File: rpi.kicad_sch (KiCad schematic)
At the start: 13 parts, among them J18 Raspberry_Pi_2_3, U1 AT24C256C, U16 MCP2518FD-xQBB, U19 SN65HVD230, Y2 40MHz

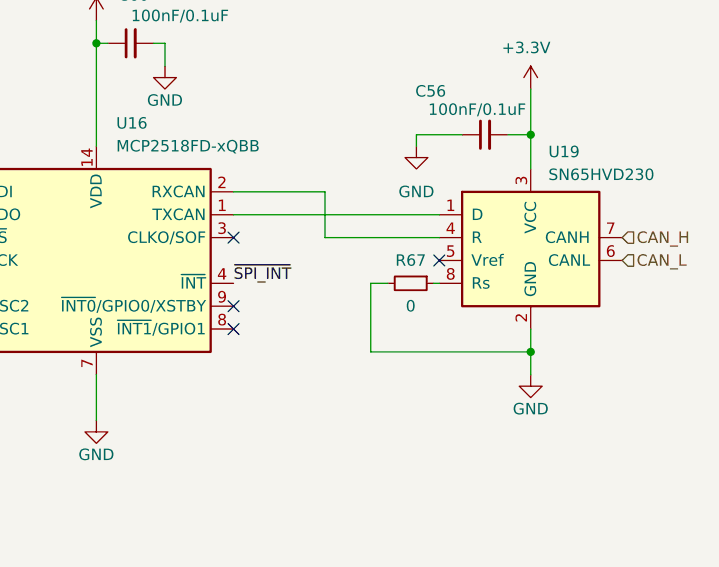
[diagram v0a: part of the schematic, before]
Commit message: Fix ERC errors
Closes #28
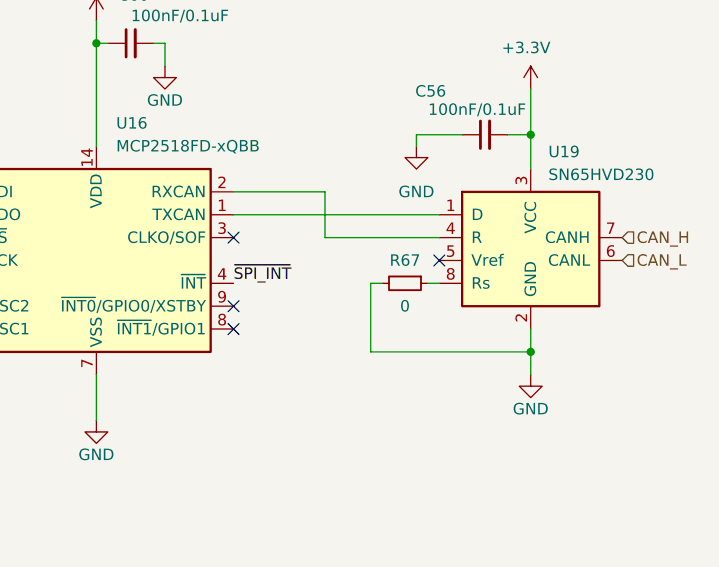
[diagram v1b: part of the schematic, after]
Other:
- moved on the sheet: R67
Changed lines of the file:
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@@
+	(wire
+		(pts
+			(xy 246.38 139.7) (xy 247.65 139.7)
+		)
+		(stroke
+			(width 0)
+			(type default)
+		)
+	)
 	(wire
 		(pts
@@
 	(wire
 		(pts
-			(xy 240.03 139.7) (xy 241.935 139.7)
+			(xy 240.03 139.7) (xy 241.3 139.7)
 		)
 		(stroke
@@
 		(pts
 			(xy 86.36 43.18) (xy 88.9 43.18)
-		)
-		(stroke
-			(width 0)
-			(type default)
-		)
-	)
-	(wire
-		(pts
-			(xy 247.015 139.7) (xy 247.65 139.7)
 		)
 		(stroke
@@
 	(symbol
 		(lib_id "Device:R_Small")
-		(at 244.475 139.7 270)
+		(at 243.84 139.7 270)
 		(unit 1)
 		(exclude_from_sim no)
@@
 		(dnp no)
 		(property "Reference" "R67"
-			(at 244.475 137.16 90)
+			(at 243.84 137.16 90)
 			(effects
 				(font
@@
 		)
 		(property "Value" "0"
-			(at 244.475 142.24 90)
+			(at 243.84 142.24 90)
 			(effects
 				(font
@@
 		)
 		(property "Footprint" "Resistor_SMD:R_0603_1608Metric"
-			(at 244.475 139.7 0)
+			(at 243.84 139.7 0)
 			(effects
 				(font
@@
 		)
 		(property "Datasheet" "~"
-			(at 244.475 139.7 0)
+			(at 243.84 139.7 0)
 			(effects
 				(font
@@
 		)
 		(property "Description" ""
-			(at 244.475 139.7 0)
+			(at 243.84 139.7 0)
 			(effects
 				(font
@@
 		)
 		(property "LCSC" "C21189"
-			(at 245.7451 142.24 0)
+			(at 245.1101 142.24 0)
 			(effects
 				(font
@@
 		)
 		(property "LCSC alt" ""
-			(at 244.475 139.7 0)
-			(effects
-				(font
+			(at 243.84 139.7 0)
+			(effects
+				(font

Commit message: Add 1-Wire
Closes #29
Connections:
- net 1WIRE: now reaches J18.7 (GCLK0/GPIO4)
- no-connect marks 30 -> 29
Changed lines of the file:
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@@
-	)
-	(no_connect
-		(at 86.36 55.88)
 	)
 	(no_connect
@@
 		(fields_autoplaced yes)
 		(effects
+			(font
+				(size 1.27 1.27)
+			)
+			(justify left)
+		)
+	)
+	(hierarchical_label "1WIRE"
+		(shape bidirectional)
+		(at 86.36 55.88 0)
+		(fields_autoplaced yes)
+		(effects

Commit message: Replace footprint for J18
Closes #31
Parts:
- J18: footprint Connector_PinSocket_2.54mm:PinSocket_2x20_P2.54mm_Vertical_SMD -> HydroponicFlowerControl:HDR-SMD_40P-P2.54-V-F-R2-C20-S7.1-EH
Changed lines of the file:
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@@
 			)
 		)
-		(property "Footprint" "Connector_PinSocket_2.54mm:PinSocket_2x20_P2.54mm_Vertical_SMD"
+		(property "Footprint" "HydroponicFlowerControl:HDR-SMD_40P-P2.54-V-F-R2-C20-S7.1-EH"
 			(at 66.04 63.5 0)
 			(effects

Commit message: Add testpoints
Closes #47
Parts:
- added TP14: ID_SCL, TestPoint:TestPoint_Pad_D1.5mm, symbol Connector:TestPoint
- added TP9: ID_SDA, TestPoint:TestPoint_Pad_D1.5mm, symbol Connector:TestPoint
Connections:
- net ID_SCL: now also TP14.1
- net ID_SDA: now also TP9.1
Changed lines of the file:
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@@
+	(wire
+		(pts
+			(xy 123.19 170.18) (xy 123.19 172.72)
+		)
+		(stroke
+			(width 0)
+			(type default)
+		)
+	)
 	(wire
 		(pts
@@
 	(wire
 		(pts
-			(xy 104.14 172.72) (xy 120.65 172.72)
+			(xy 104.14 172.72) (xy 123.19 172.72)
 		)
 		(stroke
@@
 	(wire
 		(pts
+			(xy 134.62 170.18) (xy 134.62 175.26)
+		)
+		(stroke
+			(width 0)
+			(type default)
+		)
+	)
+	(wire
+		(pts
 			(xy 179.07 143.51) (xy 180.34 143.51)
 		)
@@
 	(wire
 		(pts
-			(xy 111.76 175.26) (xy 120.65 175.26)
+			(xy 111.76 175.26) (xy 134.62 175.26)
 		)
 		(stroke
@@
 	)
 	(symbol
+		(lib_id "Connector:TestPoint")
+		(at 123.19 170.18 0)
+		(unit 1)
+		(exclude_from_sim no)
+		(in_bom yes)
+		(on_board yes)
+		(dnp no)
+		(fields_autoplaced yes)
+		(property "Reference" "TP9"
+			(at 125.73 165.6079 0)
+			(effects
+				(font
+					(size 1.27 1.27)
+				)
+				(justify left)
+			)
+		)
+		(property "Value" "ID_SDA"
+			(at 125.73 168.1479 0)
+			(effects
+				(font
+					(size 1.27 1.27)
+				)
+				(justify left)
+			)
+		)
+		(property "Footprint" "TestPoint:TestPoint_Pad_D1.5mm"
+			(at 128.27 170.18 0)
+			(effects
+				(font
+					(size 1.27 1.27)
+				)
+				(hide yes)
+			)
+		)
+		(property "Datasheet" "~"
+			(at 128.27 170.18 0)
+			(effects
+				(font
+					(size 1.27 1.27)
+				)
+				(hide yes)
+			)
+		)
+		(property "Description" "test point"
+			(at 123.19 170.18 0)
+			(effects
+				(font
+					(size 1.27 1.27)
+				)
+				(hide yes)
+			)
+		)
+		(pin "1"
+		)
+		(instances
+			(project ""
+				(path "/b3c8a28b-9ce1-4002-b8e8-ef8cb73fe031/9aca03da-9950-423c-b716-bf95878ee447"
+					(reference "TP9")
+					(unit 1)
+				)
+			)
+		)
+	)
+	(symbol
 		(lib_id "power:+5V")
 		(at 60.96 27.94 0)
@@
 					(unit 1)
 				)
+			)
+		)
+	)
+	(symbol
+		(lib_id "Connector:TestPoint")
+		(at 134.62 170.18 0)
+		(unit 1)
+		(exclude_from_sim no)
+		(in_bom yes)
+		(on_board yes)
+		(dnp no)
+		(fields_autoplaced yes)
+		(property "Reference" "TP14"
+			(at 137.16 165.6079 0)
+			(effects
+				(font
+					(size 1.27 1.27)
+				)
+				(justify left)
+			)
+		)
+		(property "Value" "ID_SCL"
+			(at 137.16 168.1479 0)
+			(effects
+				(font
+					(size 1.27 1.27)
+				)
+				(justify left)
+			)
+		)
+		(property "Footprint" "TestPoint:TestPoint_Pad_D1.5mm"
+			(at 139.7 170.18 0)
+			(effects
+				(font
+					(size 1.27 1.27)
+				)
+				(hide yes)
+			)
+		)
+		(property "Datasheet" "~"
+			(at 139.7 170.18 0)
+			(effects
+				(font
+					(size 1.27 1.27)
+				)
+				(hide yes)
+			)
+		)
+		(property "Description" "test point"
+			(at 134.62 170.18 0)
+			(effects
+				(font
+					(size 1.27 1.27)
+				)
+				(hide yes)
+			)
+		)
+		(pin "1"
+		)
+		(instances
+			(project "HydroponicFlowerControl"
+				(path "/b3c8a28b-9ce1-4002-b8e8-ef8cb73fe031/9aca03da-9950-423c-b716-bf95878ee447"
+					(reference "TP14")
+					(unit 1)
+				)

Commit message: Update manufacturing positions and rotations of parts
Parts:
- J18: JLCPCB Rotation Offset 90 -> 0
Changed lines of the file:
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@@
 			)
 		)
-		(property "JLCPCB Rotation Offset" "90"
+		(property "JLCPCB Rotation Offset" "0"
 			(at 66.04 63.5 0)
 			(effects

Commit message: Include THT components in manufacturing
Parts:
- TP14, TP9: now left out of the parts list
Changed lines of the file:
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@@
 		(unit 1)
 		(exclude_from_sim no)
-		(in_bom yes)
+		(in_bom no)
 		(on_board yes)
 		(dnp no)
@@
 		(unit 1)
 		(exclude_from_sim no)
-		(in_bom yes)
-		(on_board yes)
-		(dnp no)
+		(in_bom no)
+		(on_board yes)
+		(dnp no)
